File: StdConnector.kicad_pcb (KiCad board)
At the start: 2 copper layers, 80 x 50 mm, 52 parts, among them P1 CONN_01X02, P2 FDSP_Header, P3 StdConn_ClkOut, P4 StsConn_ClkOut, P5 StdConn_ClkVar, P6 StdConn_ClkIn, U1 74HC14, U2 LM2574, Y1 12.288MHz

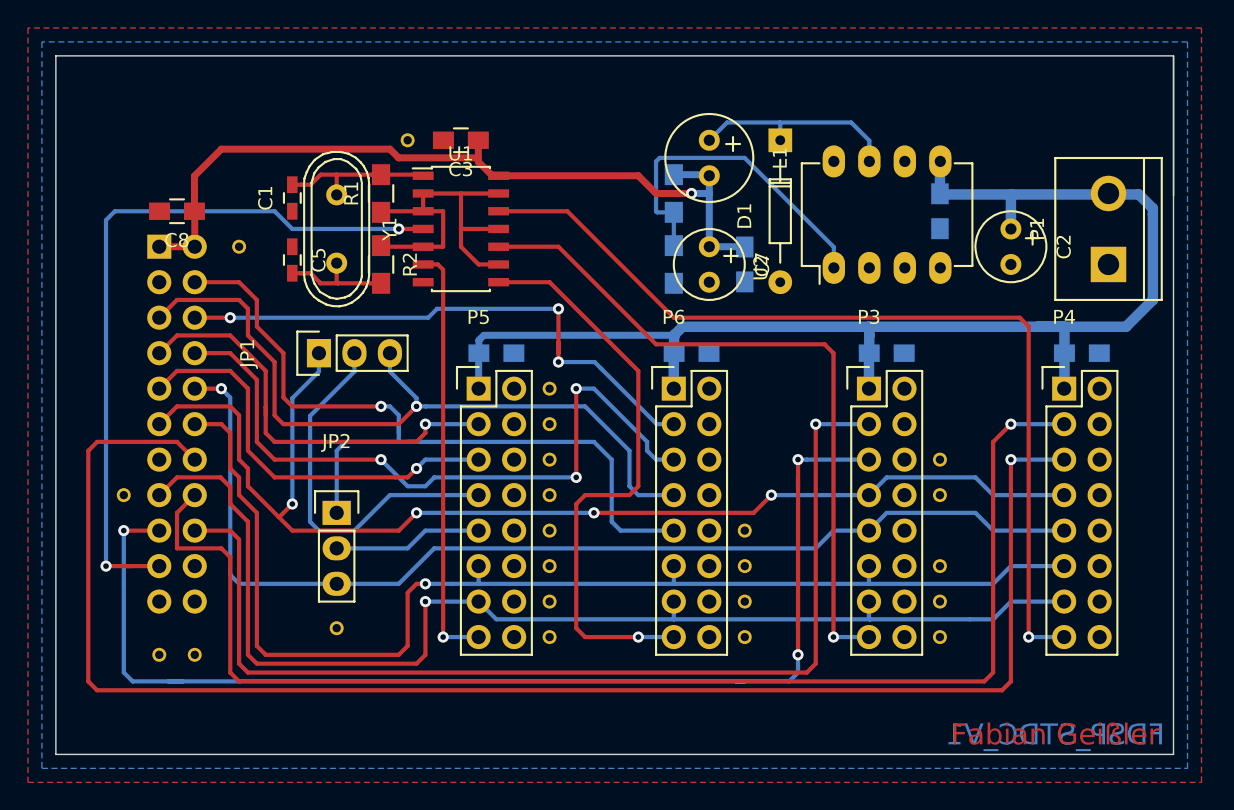
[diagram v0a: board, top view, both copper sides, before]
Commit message: Changed layout for clock lines impedance fitting to 50 ohm.
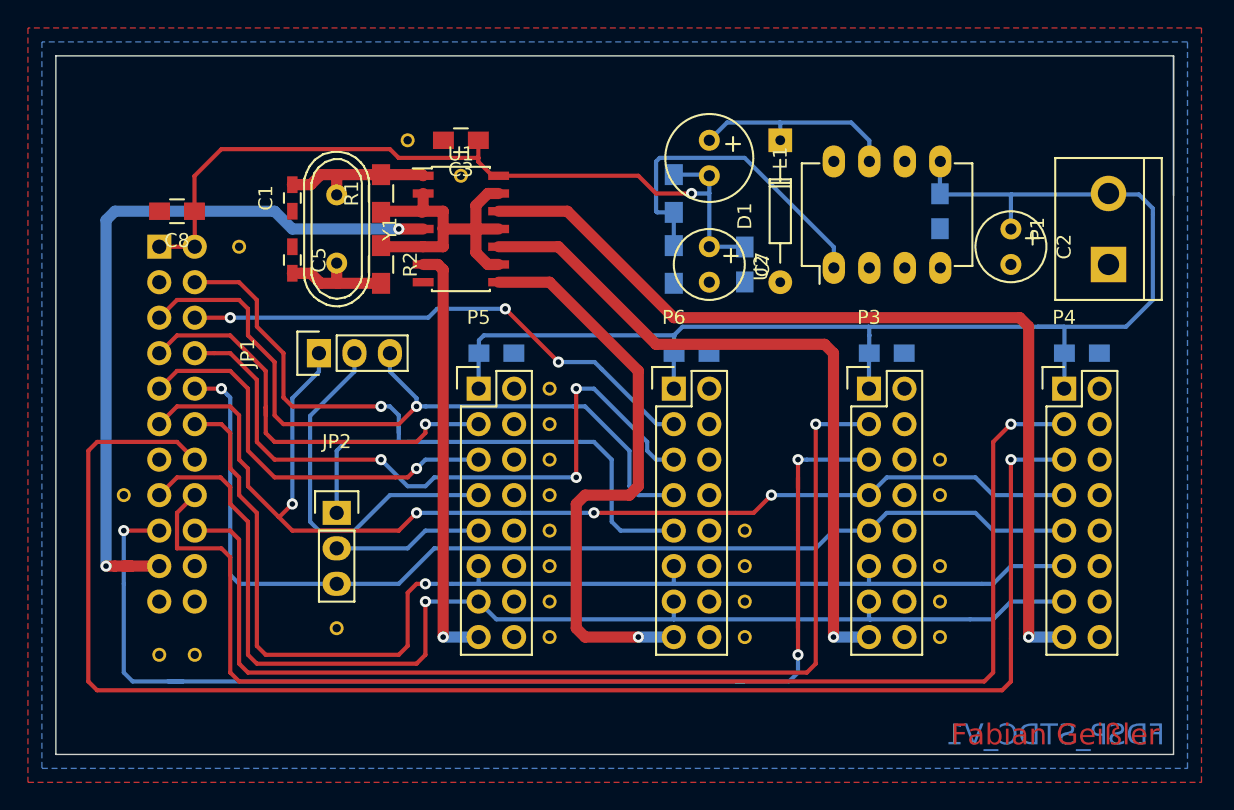
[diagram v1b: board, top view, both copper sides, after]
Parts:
- added REF**: VIA_GND, via:VIA_GND, F.Cu at (174.0, 68.6)
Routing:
- net Net-(R1-Pad1): track 28.0 -> 24.2 mm
- net /MDI1: track 41.0 -> 38.0 mm
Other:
- net class Clock added: clearance 0.15, trace_width 0.8, via_dia 0.8, via_drill 0.4

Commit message: Changed Connector position to fit old board. HF Lines optimized.
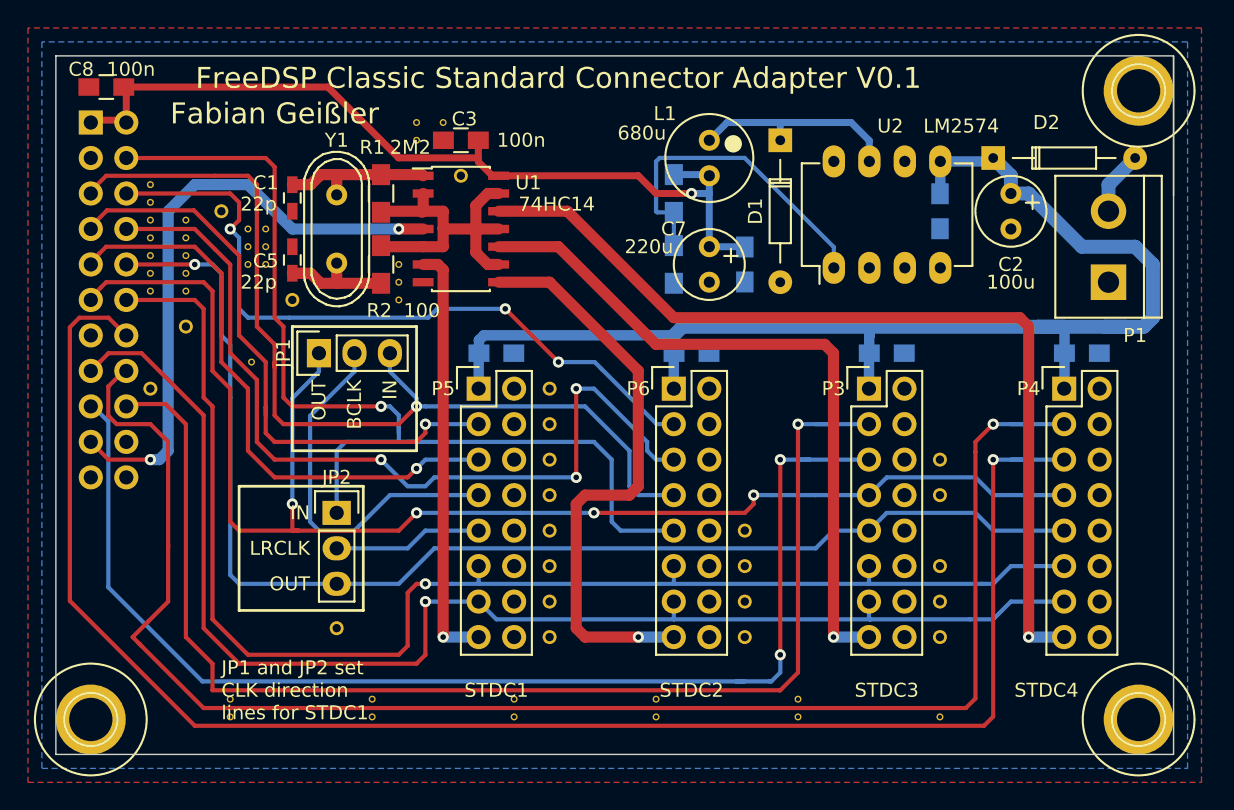
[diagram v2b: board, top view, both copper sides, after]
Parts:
- removed the REF** at (170.2, 66.0)
- removed the REF** at (152.4, 102.9)
- removed the REF** at (154.9, 102.9)
- added D2: D_Schottky, Diodes_ThroughHole:Diode_DO-35_SOD27_Horizontal_RM10, F.Cu at (212.1, 67.3)
- added REF**: VIA_GND, via:VIA_GND, F.Cu at (172.7, 64.8)
- added REF**: VIA_GND, via:VIA_GND, F.Cu at (208.3, 107.3)
- added REF**: VIA_GND, via:VIA_GND, F.Cu at (198.1, 107.3)
- added REF**: VIA_GND, via:VIA_GND, F.Cu at (188.0, 107.3)
- added REF**: VIA_GND, via:VIA_GND, F.Cu at (177.8, 107.3)
- added REF**: VIA_GND, via:VIA_GND, F.Cu at (167.6, 107.3)
- added REF**: VIA_GND, via:VIA_GND, F.Cu at (167.6, 106.0)
- added REF**: VIA_GND, via:VIA_GND, F.Cu at (157.5, 106.0)
- added REF**: VIA_GND, via:VIA_GND, F.Cu at (157.5, 107.3)
- added REF**: VIA_GND, via:VIA_GND, F.Cu at (151.8, 69.2)
- added REF**: VIA_GND, via:VIA_GND, F.Cu at (151.8, 70.5)
- added REF**: VIA_GND, via:VIA_GND, F.Cu at (170.8, 64.8)
- added REF**: VIA_GND, via:VIA_GND, F.Cu at (151.8, 76.8)
- added REF**: VIA_GND, via:VIA_GND, F.Cu at (151.8, 75.6)
- added REF**: VIA_GND, via:VIA_GND, F.Cu at (151.8, 74.3)
- added REF**: VIA_GND, via:VIA_GND, F.Cu at (151.8, 73.0)
- added REF**: VIA_GND, via:VIA_GND, F.Cu at (151.8, 71.8)
- added REF**: VIA_GND, via:VIA_GND, F.Cu at (154.3, 71.8)
- added REF**: VIA_GND, via:VIA_GND, F.Cu at (154.3, 73.0)
- added REF**: VIA_GND, via:VIA_GND, F.Cu at (154.3, 74.3)
- added REF**: VIA_GND, via:VIA_GND, F.Cu at (154.3, 75.6)
- added REF**: VIA_GND, via:VIA_GND, F.Cu at (154.3, 76.8)
- added REF**: VIA_GND, via:VIA_GND, F.Cu at (170.8, 66.0)
- added REF**: VIA_GND, via:VIA_GND, F.Cu at (159.0, 81.9)
- added REF**: VIA_GND, via:VIA_GND, F.Cu at (158.8, 74.9)
- added REF**: VIA_GND, via:VIA_GND, F.Cu at (158.8, 73.7)
- added REF**: VIA_GND, via:VIA_GND, F.Cu at (158.8, 72.4)
- added REF**: VIA_GND, via:VIA_GND, F.Cu at (160.0, 74.9)
- added REF**: VIA_GND, via:VIA_GND, F.Cu at (160.0, 73.7)
- added REF**: VIA_GND, via:VIA_GND, F.Cu at (160.0, 72.4)
- added REF**: VIA_GND, via:VIA_GND, F.Cu at (156.8, 71.1)
- added REF**: VIA_GND, via:VIA_GND, F.Cu at (151.8, 83.8)
- added REF**: 1pin, Connect:1pin, F.Cu at (222.5, 62.5)
- added REF**: VIA_GND, via:VIA_GND, F.Cu at (169.5, 77.5)
- added REF**: 1pin, Connect:1pin, F.Cu at (222.5, 107.5)
- added REF**: VIA_GND, via:VIA_GND, F.Cu at (169.5, 74.9)
- added REF**: VIA_GND, via:VIA_GND, F.Cu at (169.5, 76.2)
- added REF**: 1pin, Connect:1pin, F.Cu at (147.5, 107.5)
- added REF**: VIA_GND, via:VIA_GND, F.Cu at (198.1, 106.0)
- added REF**: VIA_GND, via:VIA_GND, F.Cu at (188.0, 106.0)
- added REF**: VIA_GND, via:VIA_GND, F.Cu at (177.8, 106.0)
- moved REF** 12.9 mm to (154.3, 79.4)
- moved C8 10.2 mm to (148.6, 62.2)
- moved P2 10.2 mm to (147.5, 64.8)
- moved REF** 5.39 mm to (161.9, 77.5)
- moved C2 2.54 mm to (213.4, 69.8)
- moved P1 1.27 mm to (220.3, 73.7)
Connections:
- net +3V3 renamed VCC
- P1 pad 2: +12V -> Net-(D2-Pad2)
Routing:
- net /MDI3: track 93.9 -> 113.3 mm
- net /BCLK_OUT: track 86.6 -> 102.8 mm
- net /MDI2: track 75.1 -> 91.1 mm
- net /LRCLK_IN: track 58.7 -> 73.6 mm
- net /BCLK_IN: track 53.6 -> 68.1 mm
- net /MDI1: track 38.0 -> 51.5 mm
- net /LRCLK_OUT: track 78.1 -> 91.6 mm
- net /SDA: track 85.6 -> 99.1 mm
- net /MDO1: track 49.9 -> 62.2 mm
- net /MDI0: track 30.6 -> 42.9 mm
- net /MDO0: track 29.7 -> 41.9 mm
- net /SCL: track 84.9 -> 96.1 mm
- net /MCLK: track 52.6 -> 43.8 mm
- net /MDO3: track 111.2 -> 119.0 mm
- net Net-(D2-Pad2): track 0.00 -> 4.60 mm
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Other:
- net class P12V added: clearance 0.15, trace_width 0.75, via_dia 0.8, via_drill 0.4
- net class P3V3 added: clearance 0.15, trace_width 0.5, via_dia 0.8, via_drill 0.4
- board text added: "BCLK"
- board text added: "FreeDSP Classic Standard Connector Adapter V0.1"
- board text added: "IN"
- board text added: "JP1 and JP2 set CLK direction lines for STDC1"
- board text added: "LRCLK"
- board text added: "OUT"
- board text added: "STDC1"
- board text added: "STDC2"
- board text added: "STDC3"
- board text added: "STDC4"
- board text removed: "FDSP_STDC_V1"

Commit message: Made all GND VIAs equal size.
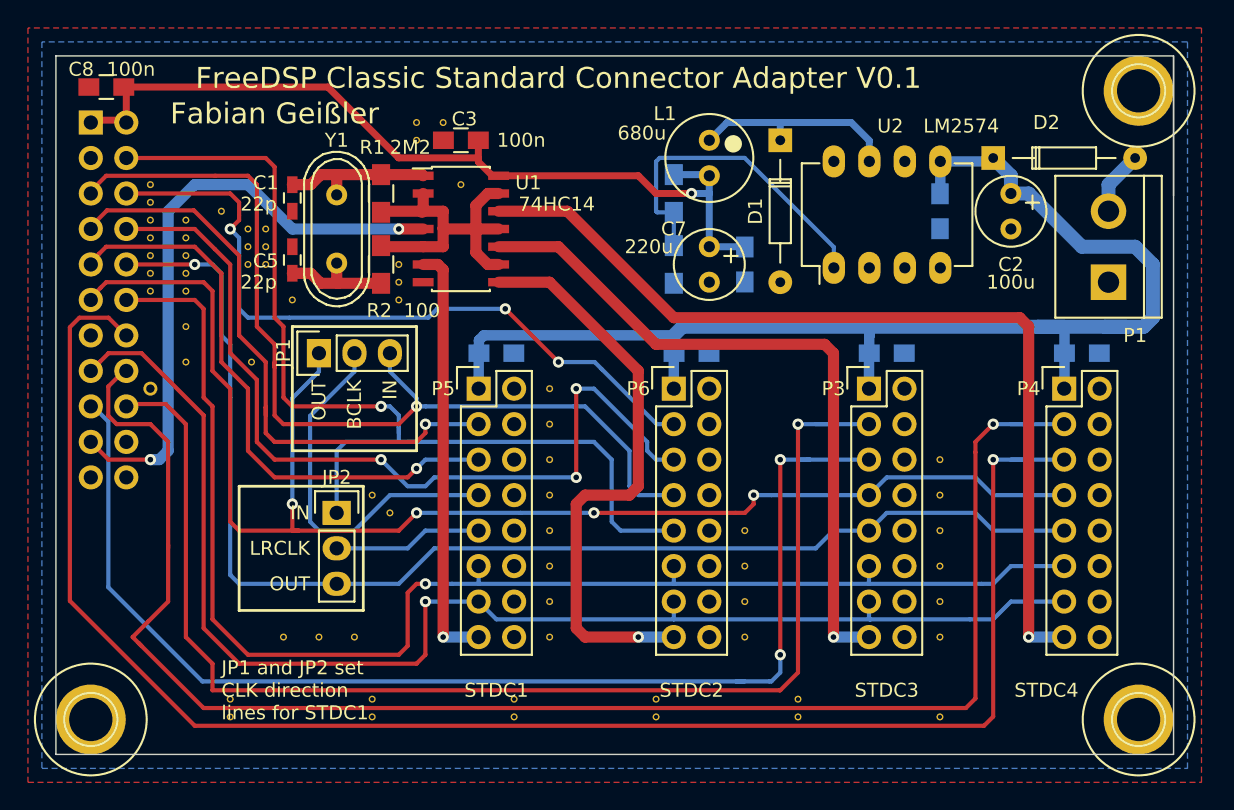
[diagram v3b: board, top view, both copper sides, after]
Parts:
- removed the REF** at (174.0, 68.6)
- removed the REF** at (165.1, 101.0)
- added REF**: VIA_GND, via:VIA_GND, F.Cu at (154.3, 81.9)
- added REF**: VIA_GND, via:VIA_GND, F.Cu at (168.9, 92.7)
- added REF**: VIA_GND, via:VIA_GND, F.Cu at (167.6, 91.4)
- added REF**: VIA_GND, via:VIA_GND, F.Cu at (174.0, 69.2)
- added REF**: VIA_GND, via:VIA_GND, F.Cu at (166.4, 101.6)
- added REF**: VIA_GND, via:VIA_GND, F.Cu at (163.8, 101.6)
- added REF**: VIA_GND, via:VIA_GND, F.Cu at (161.3, 101.6)
- added REF**: VIA_GND, via:VIA_GND, F.Cu at (208.3, 94.0)

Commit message: Corrected resistor value error in stepdown feedback.
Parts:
- R3: value 1k3 -> 3k3
- R4: value 2k2 -> 2k
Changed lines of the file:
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@@
     (links 190)
     (no_connects 0)
-    (area 143 56.345 230.483334 113.505)
+    (area 144.949999 59.949999 225.050001 110.050001)
     (thickness 1.6)
     (drawings 27)
@@
       (effects (font (size 1 1) (thickness 0.15)) (justify mirror))
     )
-    (fp_text value 1k3 (at 0.254 2.286 360) (layer B.SilkS)
+    (fp_text value 3k3 (at 0.254 2.286 360) (layer B.SilkS)
       (effects (font (size 1 1) (thickness 0.15)) (justify mirror))
     )
@@
       (effects (font (size 1 1) (thickness 0.15)) (justify mirror))
     )
-    (fp_text value 2k2 (at 0 2.286 360) (layer B.SilkS)
+    (fp_text value 2k (at 0 2.286 360) (layer B.SilkS)
       (effects (font (size 1 1) (thickness 0.15)) (justify mirror))
     )

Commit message: Little Changes, added Gerber files.
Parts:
- removed the REF** at (222.5, 62.5)
- removed the REF** at (222.5, 107.5)
- removed the REF** at (147.5, 107.5)
- added G***: LOGO, LOGO, F.Cu at (158.5, 65.2)
- added G***: LOGO, LOGO, B.Cu at (184.9, 99.1)
- added REF**: Hole_M3, fdsp_mechanical:Hole_M3, F.Cu at (222.5, 62.5)
- added REF**: VIA_GND, via:VIA_GND, F.Cu at (189.2, 76.3)
- added REF**: VIA_GND, via:VIA_GND, F.Cu at (194.3, 76.2)
- added REF**: Hole_M3, fdsp_mechanical:Hole_M3, F.Cu at (222.5, 107.5)
- added REF**: VIA_GND, via:VIA_GND, F.Cu at (210.2, 72.4)
- added REF**: VIA_GND, via:VIA_GND, F.Cu at (206.4, 72.4)
- added REF**: VIA_GND, via:VIA_GND, F.Cu at (208.3, 72.4)
- added REF**: VIA_GND, via:VIA_GND, F.Cu at (195.6, 77.5)
- added REF**: VIA_GND, via:VIA_GND, F.Cu at (193.0, 77.5)
- added REF**: Hole_M3, fdsp_mechanical:Hole_M3, F.Cu at (147.5, 107.5)
- added REF**: VIA_GND, via:VIA_GND, F.Cu at (190.5, 77.5)
- added REF**: VIA_GND, via:VIA_GND, F.Cu at (187.3, 74.9)
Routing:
- added copper zone on B.Cu, net +12V
- added copper zone on B.Cu, net Net-(D1-Pad1)
- added copper zone on B.Cu, net VCC
